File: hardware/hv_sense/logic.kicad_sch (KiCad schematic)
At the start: 32 parts, among them U1 4081, U2 4071, U3 4081, U4 40106, U5 40106, U6 4013

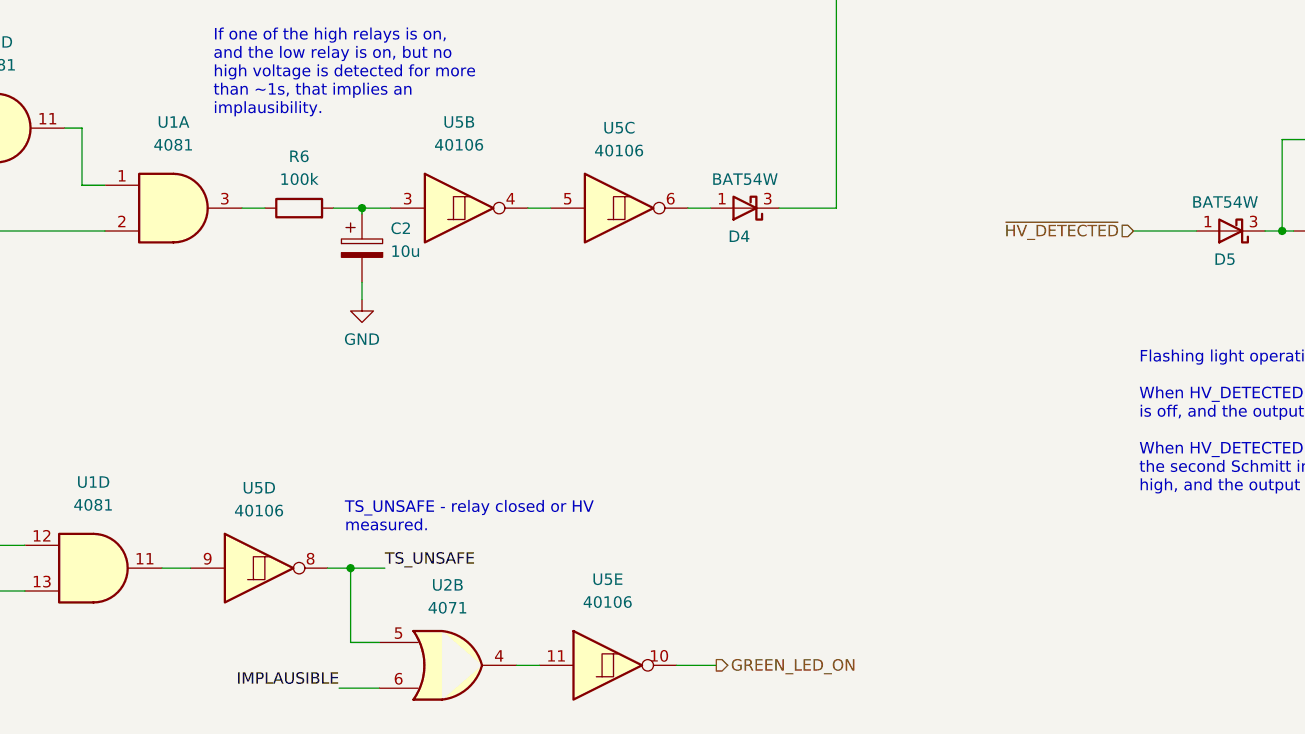
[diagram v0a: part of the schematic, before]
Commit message: Added switch to choose between FSG and FSUK rules
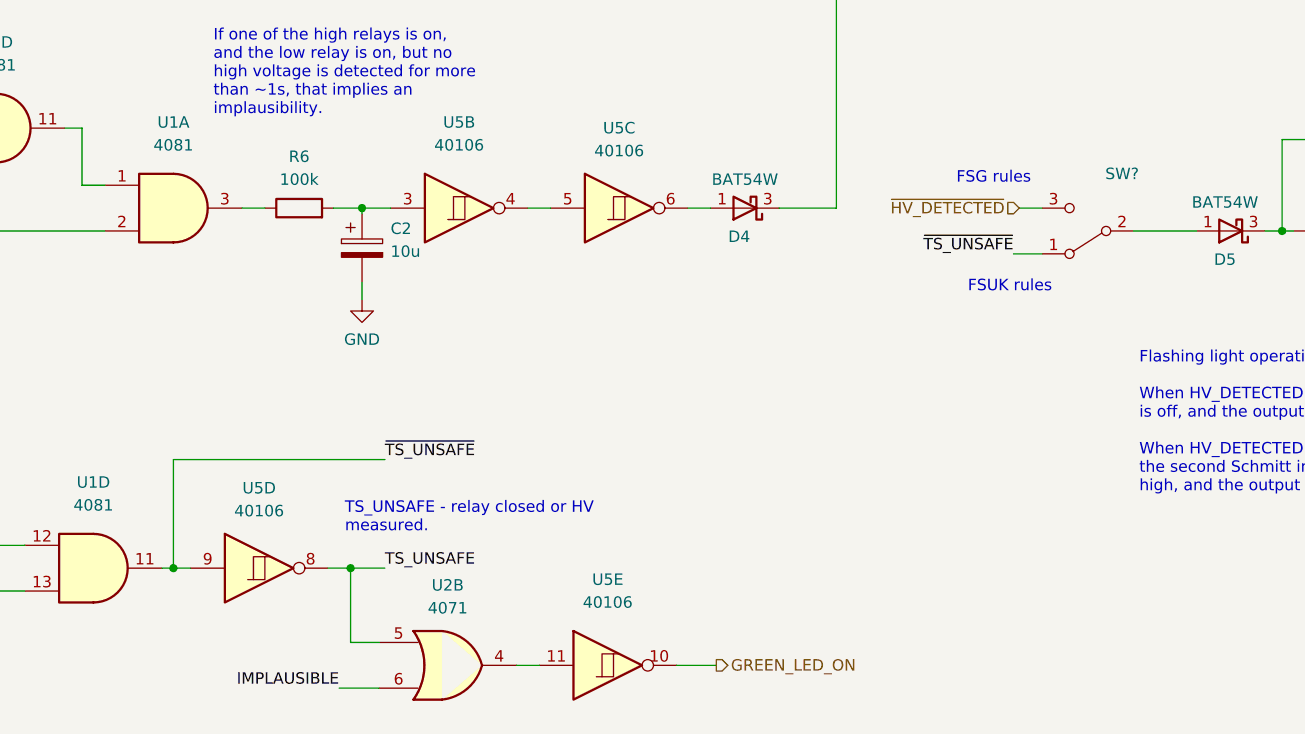
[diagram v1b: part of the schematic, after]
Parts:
- added SW?: (no value), symbol Switch:SW_SPDT
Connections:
- net ~{HV_DETECTED}: now also SW?.3 (C); no longer D5.1 (A)
- net ~{TS_UNSAFE}: now reaches U1.11, U5.9
- net ~{TS_UNSAFE}: now also SW?.1 (A)
- new net: D5.1 (A), SW?.2 (B)
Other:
- note added: "FSG rules"
- note added: "FSUK rules"
